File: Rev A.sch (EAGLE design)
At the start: 91 parts, among them IC301 LM339N, Q1 2N3906, Q10 2N3906, Q1001 2N3904, Q1002 2N3906, Q11 2N3906, Q12 2N3904, Q13 2N3904, Q14 2N3904, Q15 TIP41C, Q16 TIP42C, Q2 2N3906, Q3 2N3904, Q4 2N3904, Q5 2N3904, Q6 TIP41C, Q7 TIP42C, Q8 2N3904, Q9 2N3906

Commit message: Renumbering
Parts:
- renumbered C1 to C106, C1001 to C105, C1002 to C101, C1003 to C102, C2 to C103, C3 to C104, D1 to D102, D1001 to D105, D2 to D101, D3 to D106, D4 to D107, D5 to D104, D6 to D103, D7 to D108, F1 to F201, F2 to F202, IC301 to IC201, L_OUT1 to L_OUT101, L_OUT2 to L_OUT102, Q1 to Q101, Q10 to Q102, Q1001 to Q111, Q1002 to Q112, Q11 to Q108, Q12 to Q106, Q13 to Q104, Q14 to Q110, Q15 to Q118, Q16 to Q117, Q2 to Q107, Q3 to Q105, Q4 to Q103, Q5 to Q109, Q6 to Q116, Q7 to Q115, Q8 to Q113, Q9 to Q114, R1 to R101, R10 to R102, R11 to R104, R12 to R110, R13 to R113, R14 to R117, R15 to R114, R16 to R106, R17 to R108, R18 to R118, R2 to R103, R3 to R109, R4 to R111, R5 to R115, R6 to R116, R7 to R112, R8 to R105, R9 to R107, R_OUT1 to R_OUT101, R_OUT2 to R_OUT102
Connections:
- net GND: now also C203.+, C204.-; no longer C203.-, C204.+
- net V+: now also C204.+; no longer C203.+
- net V-: now also C203.-; no longer C204.-

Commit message: Fixed the reversed JST connectors
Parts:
- removed L_OUT101, L_OUT102, PWR+, PWR-, R_OUT101, R_OUT102: (no value), adafruit:JST_2PIN-THM
- added L_OUT1, L_OUT2, PWR+1, PWR+2, PWR-1, PWR-2, R_OUT1, R_OUT2: (no value), adafruit:JST_2PIN-THM
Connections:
- net GND: now also L_IN.1, L_OUT1.1, L_OUT2.1, PWR+1.1, PWR+2.1, PWR-1.2, PWR-2.2, R_IN.1, R_OUT1.1, R_OUT2.1; no longer L_IN.2, L_OUT101.2, L_OUT102.2, PWR+.2, PWR-.1, R_IN.2, R_OUT101.2, R_OUT102.2
- net L_OUT: now also L_OUT1.2, L_OUT2.2; no longer L_OUT101.1, L_OUT102.1
- net N$30: now also L_IN.2; no longer L_IN.1
- net N$43: now also PWR+1.2, PWR+2.2; no longer PWR+.1
- net N$44: now also PWR-1.1, PWR-2.1; no longer PWR-.2
- net N$6: now also R_IN.2; no longer R_IN.1
- net R_OUT: now also R_OUT1.2, R_OUT2.2; no longer R_OUT101.1, R_OUT102.1
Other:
- moved on the sheet: F201, F202, L_IN, R_IN

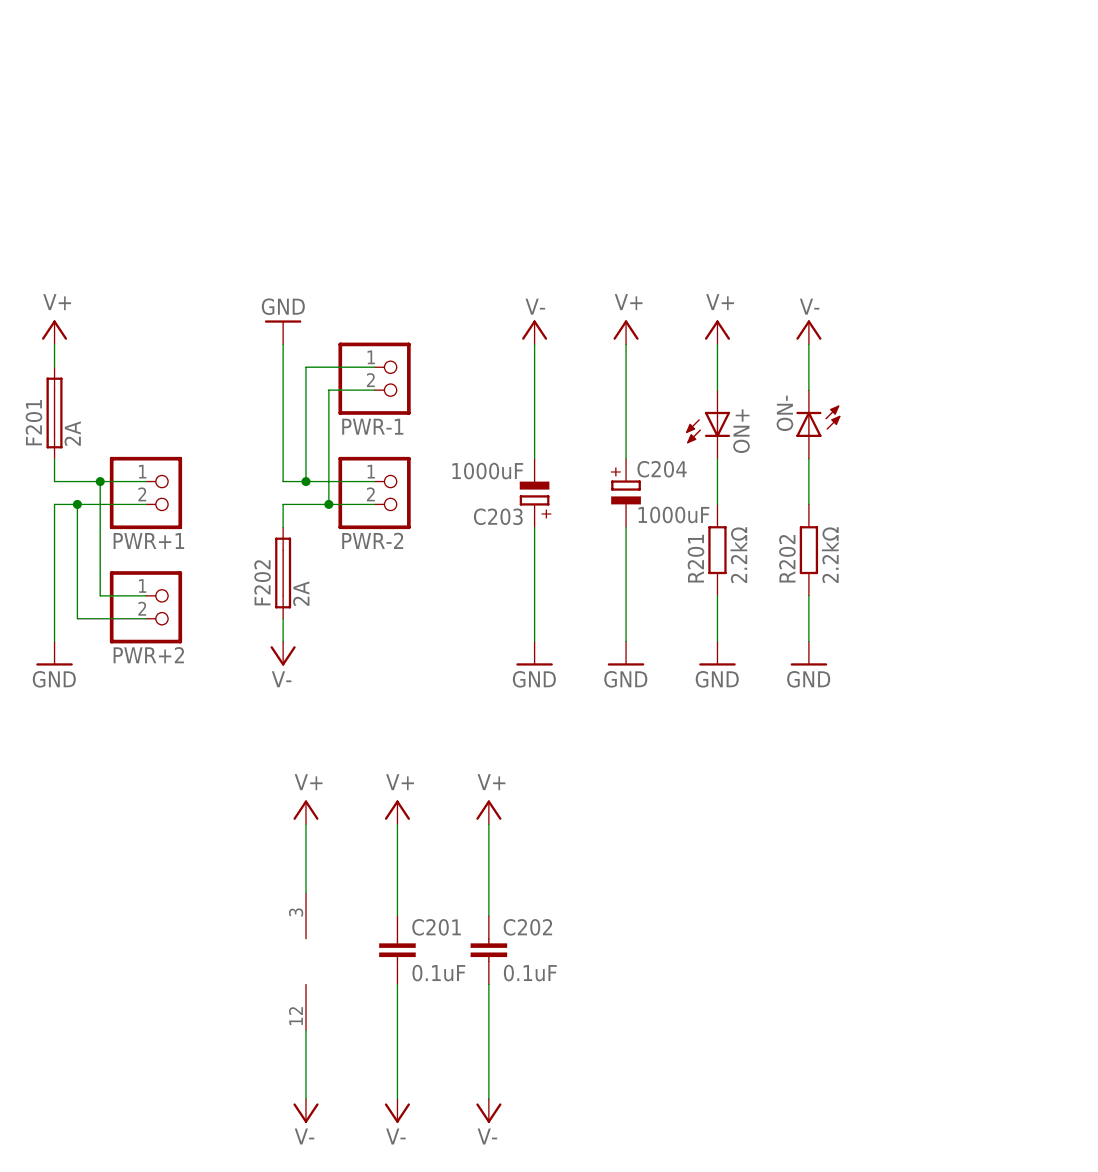
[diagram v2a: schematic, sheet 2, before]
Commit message: Made some changes to the connector arrangement in the power supply
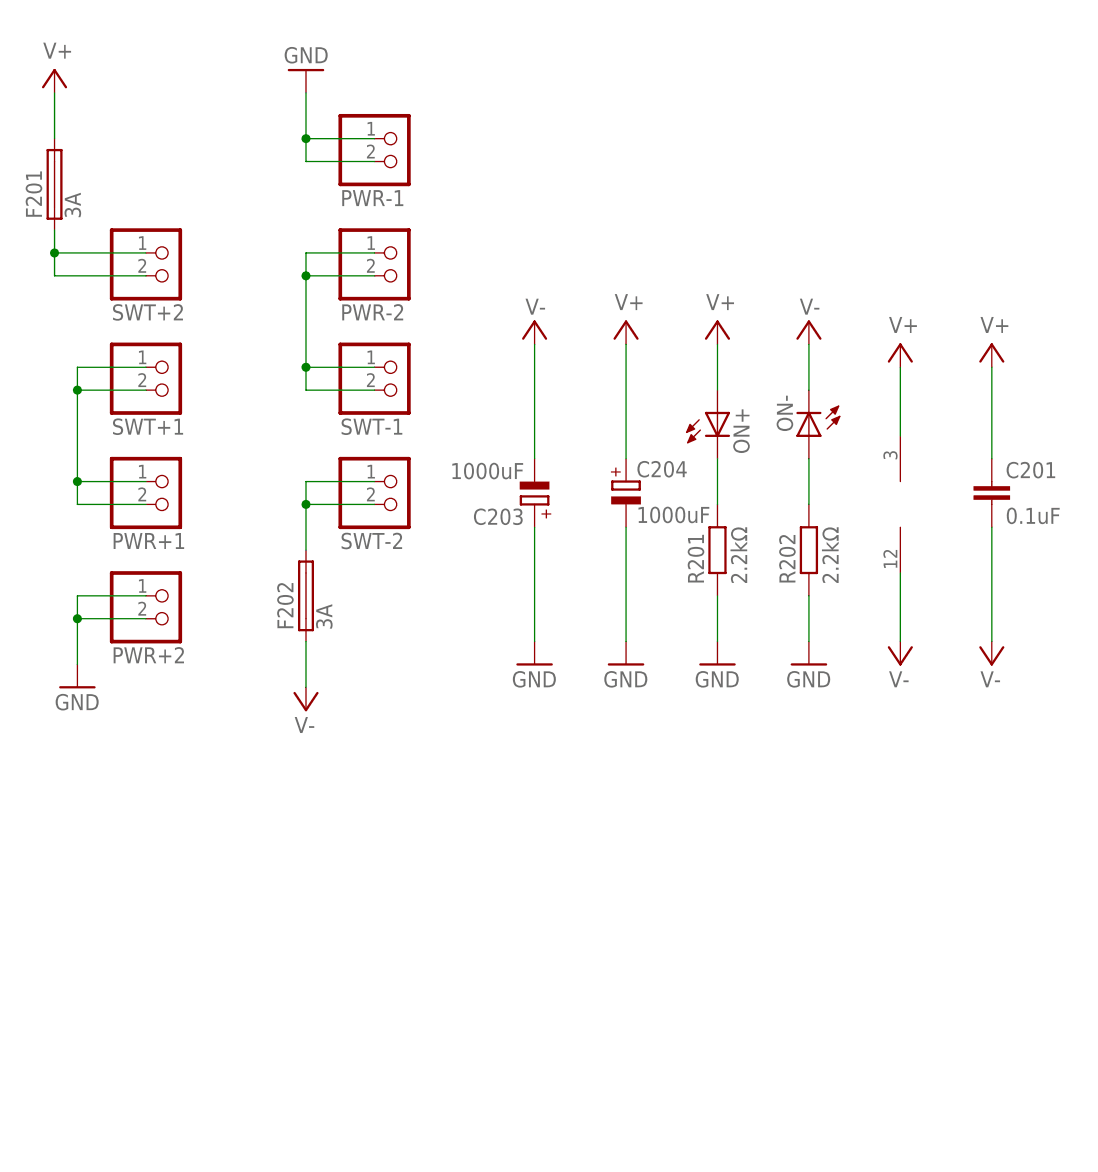
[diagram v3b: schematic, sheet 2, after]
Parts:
- removed C202: 0.1uF, rcl:C-EU025-025X050
- added SWT+1, SWT+2, SWT-1, SWT-2: (no value), adafruit:JST_2PIN-THM
- F201, F202: value 2A -> 3A
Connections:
- new net N$45: F202.2, SWT-2.1, SWT-2.2
- new net N$47: F201.1, SWT+2.1, SWT+2.2
- net GND: now also PWR+2.2, PWR-1.1; no longer PWR+1.1, PWR-2.2
- net N$43: now also PWR+1.1, SWT+1.1, SWT+1.2; no longer F201.1, PWR+2.2
- net N$44: now also PWR-2.2, SWT-1.1, SWT-1.2; no longer F202.2, PWR-1.1
- net V+: no longer C202.1
- net V-: no longer C202.2
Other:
- moved on the sheet: C201, F201, F202, PWR-1, PWR-2

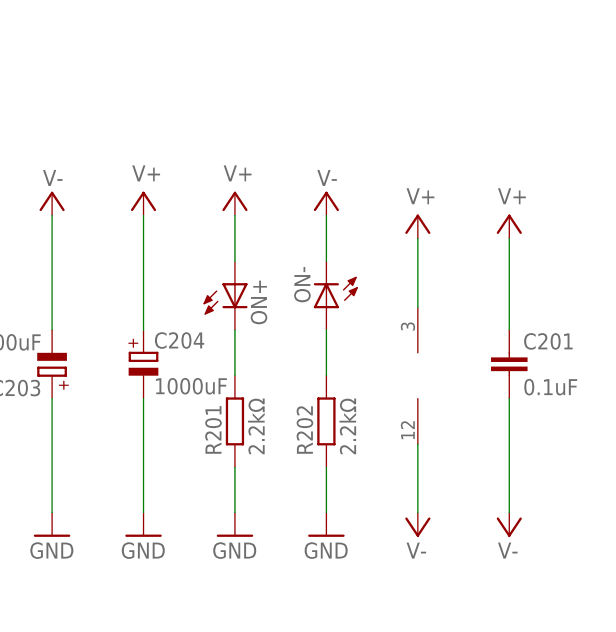
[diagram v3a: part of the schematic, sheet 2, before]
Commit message: Removed one LED
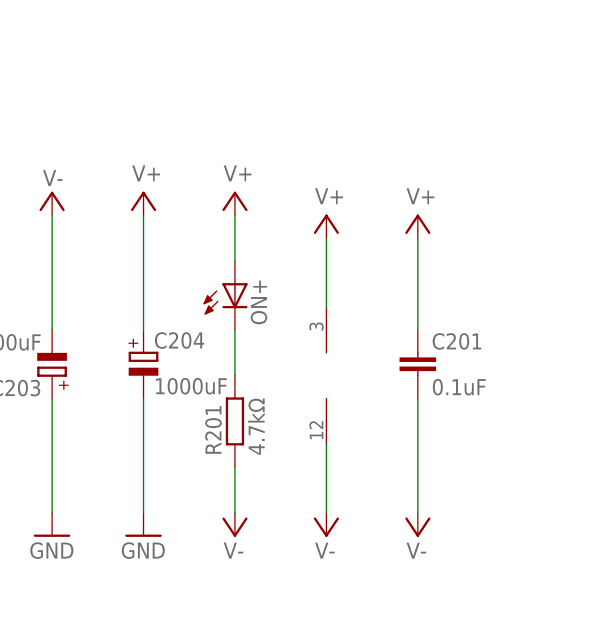
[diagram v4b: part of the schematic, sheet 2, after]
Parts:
- removed ON-: (no value), led:LEDSQR2X5
- removed R202: 2.2kΩ, rcl:R-EU_0207/10
- R201: value 2.2kΩ -> 4.7kΩ
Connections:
- removed net N$7: ON-.A, R202.2
- net GND: no longer R201.1, R202.1
- net V-: now also R201.1; no longer ON-.C
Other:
- moved on the sheet: C201
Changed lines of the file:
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@@
 <part name="GND13" library="supply1" deviceset="GND" device=""/>
 <part name="ON+" library="led" deviceset="LED" device="SQR2X5"/>
-<part name="R201" library="rcl" deviceset="R-EU_" device="0207/10" value="2.2kΩ"/>
-<part name="GND8" library="supply1" deviceset="GND" device=""/>
+<part name="R201" library="rcl" deviceset="R-EU_" device="0207/10" value="4.7kΩ"/>
 <part name="GND3" library="supply1" deviceset="GND" device=""/>
 <part name="SUPPLY5" library="supply2" deviceset="V+" device=""/>
@@
 <part name="SUPPLY8" library="supply2" deviceset="V+" device=""/>
 <part name="SUPPLY9" library="supply2" deviceset="V+" device=""/>
-<part name="R202" library="rcl" deviceset="R-EU_" device="0207/10" value="2.2kΩ"/>
-<part name="GND12" library="supply1" deviceset="GND" device=""/>
-<part name="ON-" library="led" deviceset="LED" device="SQR2X5"/>
-<part name="SUPPLY10" library="supply2" deviceset="V-" device=""/>
 <part name="SUPPLY11" library="supply2" deviceset="V+" device=""/>
 <part name="GND14" library="supply1" deviceset="GND" device=""/>
@@
 <part name="SWT-1" library="adafruit" deviceset="JST_2PIN" device="-THM"/>
 <part name="SWT-2" library="adafruit" deviceset="JST_2PIN" device="-THM"/>
+<part name="SUPPLY10" library="supply2" deviceset="V-" device=""/>
 </parts>
 <sheets>
@@
 <instance part="ON+" gate="G$1" x="71.12" y="83.82"/>
 <instance part="R201" gate="G$1" x="71.12" y="68.58" rot="R90"/>
-<instance part="GND8" gate="1" x="71.12" y="55.88"/>
 <instance part="GND3" gate="1" x="0" y="53.34"/>
-<instance part="SUPPLY5" gate="1" x="91.44" y="91.44"/>
-<instance part="SUPPLY6" gate="1" x="91.44" y="55.88"/>
+<instance part="SUPPLY5" gate="1" x="81.28" y="91.44"/>
+<instance part="SUPPLY6" gate="1" x="81.28" y="55.88"/>
 <instance part="GND6" gate="1" x="50.8" y="55.88"/>
 <instance part="SUPPLY7" gate="1" x="50.8" y="93.98" rot="R180"/>
 <instance part="SUPPLY8" gate="1" x="60.96" y="93.98"/>
 <instance part="SUPPLY9" gate="1" x="71.12" y="93.98"/>
-<instance part="R202" gate="G$1" x="81.28" y="68.58" rot="R90"/>
-<instance part="GND12" gate="1" x="81.28" y="55.88"/>
-<instance part="ON-" gate="G$1" x="81.28" y="81.28" rot="R180"/>
-<instance part="SUPPLY10" gate="1" x="81.28" y="93.98" rot="R180"/>
 <instance part="SUPPLY11" gate="1" x="-2.54" y="121.92"/>
 <instance part="GND14" gate="1" x="25.4" y="121.92" rot="R180"/>
 <instance part="SUPPLY12" gate="1" x="25.4" y="50.8"/>
-<instance part="C201" gate="G$1" x="101.6" y="76.2"/>
-<instance part="SUPPLY13" gate="1" x="101.6" y="91.44"/>
-<instance part="SUPPLY14" gate="1" x="101.6" y="55.88"/>
+<instance part="C201" gate="G$1" x="91.44" y="76.2"/>
+<instance part="SUPPLY13" gate="1" x="91.44" y="91.44"/>
+<instance part="SUPPLY14" gate="1" x="91.44" y="55.88"/>
 <instance part="C204" gate="G$1" x="60.96" y="76.2"/>
 <instance part="C203" gate="G$1" x="50.8" y="73.66" rot="R180"/>
-<instance part="IC201" gate="P" x="91.44" y="73.66"/>
+<instance part="IC201" gate="P" x="81.28" y="73.66"/>
 <instance part="F201" gate="1" x="-2.54" y="109.22" rot="R90"/>
 <instance part="F202" gate="1" x="25.4" y="63.5" rot="R90"/>
@@
 <instance part="SWT-1" gate="G$1" x="35.56" y="88.9" rot="MR180"/>
 <instance part="SWT-2" gate="G$1" x="35.56" y="76.2" rot="MR180"/>
+<instance part="SUPPLY10" gate="1" x="71.12" y="55.88"/>
 </instances>
 <busses>
@@
 </segment>
 <segment>
-<pinref part="R201" gate="G$1" pin="1"/>
-<wire x1="71.12" y1="63.5" x2="71.12" y2="58.42" width="0.1524" layer="91"/>
-<pinref part="GND8" gate="1" pin="GND"/>
-</segment>
-<segment>
 <wire x1="50.8" y1="71.12" x2="50.8" y2="58.42" width="0.1524" layer="91"/>
 <pinref part="GND6" gate="1" pin="GND"/>
 <pinref part="C203" gate="G$1" pin="+"/>
-</segment>
-<segment>
-<pinref part="R202" gate="G$1" pin="1"/>
-<wire x1="81.28" y1="63.5" x2="81.28" y2="58.42" width="0.1524" layer="91"/>
-<pinref part="GND12" gate="1" pin="GND"/>
 </segment>
 <segment>
@@
 <segment>
 <pinref part="SUPPLY6" gate="1" pin="V-"/>
-<wire x1="91.44" y1="66.04" x2="91.44" y2="58.42" width="0.1524" layer="91"/>
+<wire x1="81.28" y1="66.04" x2="81.28" y2="58.42" width="0.1524" layer="91"/>
 <pinref part="IC201" gate="P" pin="GND"/>
 </segment>
@@
 </segment>
 <segment>
-<wire x1="81.28" y1="86.36" x2="81.28" y2="91.44" width="0.1524" layer="91"/>
-<pinref part="ON-" gate="G$1" pin="C"/>
-<pinref part="SUPPLY10" gate="1" pin="V-"/>
-</segment>
-<segment>
 <pinref part="SUPPLY14" gate="1" pin="V-"/>
 <pinref part="C201" gate="G$1" pin="2"/>
-<wire x1="101.6" y1="58.42" x2="101.6" y2="71.12" width="0.1524" layer="91"/>
+<wire x1="91.44" y1="58.42" x2="91.44" y2="71.12" width="0.1524" layer="91"/>
 </segment>
 <segment>
@@
 <wire x1="25.4" y1="53.34" x2="25.4" y2="58.42" width="0.1524" layer="91"/>
 </segment>
+<segment>
+<pinref part="R201" gate="G$1" pin="1"/>
+<wire x1="71.12" y1="63.5" x2="71.12" y2="58.42" width="0.1524" layer="91"/>
+<pinref part="SUPPLY10" gate="1" pin="V-"/>
+</segment>
 </net>
 <net name="V+" class="0">
 <segment>
 <pinref part="SUPPLY5" gate="1" pin="V+"/>
-<wire x1="91.44" y1="88.9" x2="91.44" y2="81.28" width="0.1524" layer="91"/>
+<wire x1="81.28" y1="88.9" x2="81.28" y2="81.28" width="0.1524" layer="91"/>
 <pinref part="IC201" gate="P" pin="V+"/>
 </segment>
@@
 <pinref part="C201" gate="G$1" pin="1"/>
 <pinref part="SUPPLY13" gate="1" pin="V+"/>
-<wire x1="101.6" y1="78.74" x2="101.6" y2="88.9" width="0.1524" layer="91"/>
+<wire x1="91.44" y1="78.74" x2="91.44" y2="88.9" width="0.1524" layer="91"/>
 </segment>
 <segment>
@@
 </segment>
 </net>
-<net name="N$7" class="0">
-<segment>
-<wire x1="81.28" y1="78.74" x2="81.28" y2="73.66" width="0.1524" layer="91"/>
-<pinref part="R202" gate="G$1" pin="2"/>
-<pinref part="ON-" gate="G$1" pin="A"/>
-</segment>
-</net>

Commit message: Made major changes to the schematic
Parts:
- removed C201: 0.1uF, rcl:C-EU025-025X050
- removed C301, C302: 10uF, rcl:CPOL-EUE2.5-6
- removed D301, D302: 6.2V, diode:ZENER-DIODEDO34-7
- removed IC201: LM339N, linear:LM339N
- removed L_CLIP, R_CLIP: (no value), adafruit:LED5MM
- removed ON+: (no value), led:LEDSQR2X5
- removed R301, R302, R303, R304: 10kΩ, rcl:R-EU_0207/10
- removed R305, R306: 1kΩ, rcl:R-EU_0207/10
- removed R307, R308, R310, R312: 100kΩ, rcl:R-EU_0207/10
- removed R309, R311: 56kΩ, rcl:R-EU_0207/10
- removed R313, R314: 2.2kΩ, rcl:R-EU_0207/10
- removed VR301, VR302: 10kΩ, bourns:3362U
- added LED: (no value), adafruit:JST_2PIN-THM
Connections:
- removed net N$10: IC201A.+IN, VR301.2
- removed net N$11: D301.C, R305.1, VR301.1
- removed net N$12: C301.+, IC201A.OUT, IC201B.-IN, R307.1
- removed net N$13: IC201B.+IN, R309.1, R310.2
- removed net N$14: IC201B.OUT, R_CLIP.C
- removed net N$15: R313.1, R_CLIP.A
- removed net N$16: IC201C.-IN, R302.2, R304.1
- removed net N$17: IC201C.+IN, VR302.2
- removed net N$18: D302.C, R306.1, VR302.1
- removed net N$19: C302.+, IC201C.OUT, IC201D.-IN, R308.1
- removed net N$20: IC201D.+IN, R311.1, R312.2
- removed net N$21: IC201D.OUT, L_CLIP.C
- removed net N$23: L_CLIP.A, R314.1
- removed net N$9: IC201A.-IN, R301.2, R303.1
- net GND: now also L_OUT2.2, R_OUT2.2; no longer D301.A, D302.A, L_OUT1.1, R303.2, R304.2, R_OUT1.1, VR301.3, VR302.3
- net L_OUT: now also L_OUT1.1; no longer L_OUT2.2, R302.1
- net N$22: now also LED.1; no longer ON+.C
- net R_OUT: now also R_OUT1.1; no longer R301.1, R_OUT2.2
- net V+: now also LED.2; no longer C201.1, IC201P.V+, ON+.A, R305.2, R306.2, R307.2, R308.2, R309.2, R311.2, R313.2, R314.2
- net V-: no longer C201.2, C301.-, C302.-, IC201P.GND, R310.1, R312.1
